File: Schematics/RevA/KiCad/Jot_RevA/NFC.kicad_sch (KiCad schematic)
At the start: 0 parts

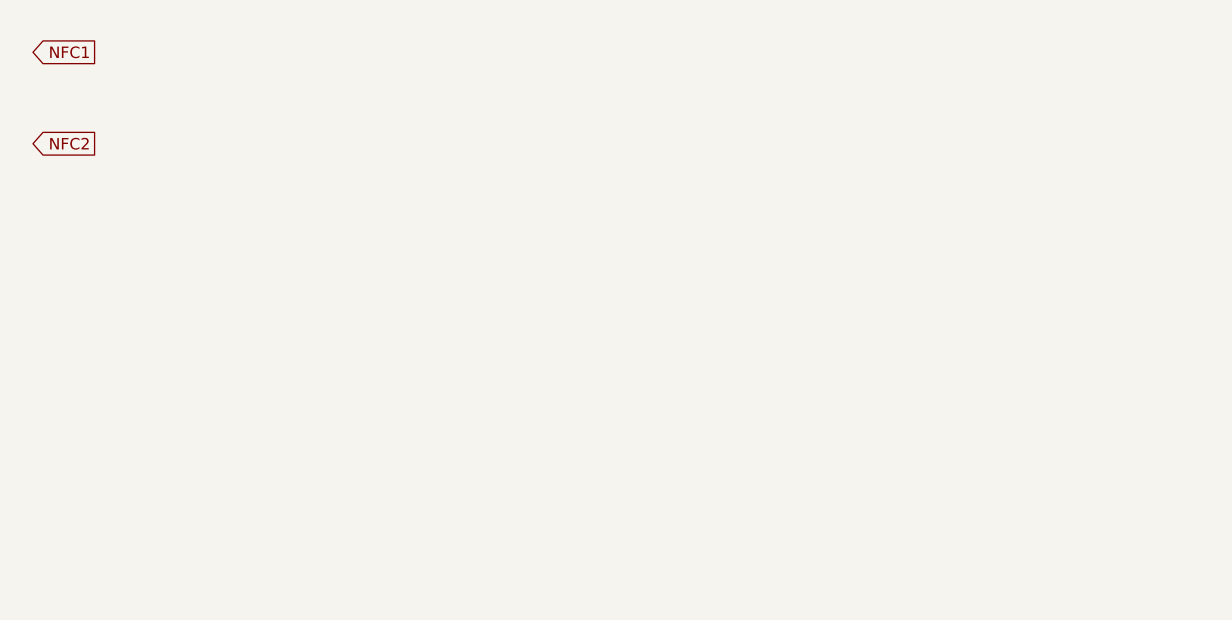
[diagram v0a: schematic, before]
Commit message: NFC sheet: AE1 PCB coil across NFC1/NFC2, C16/C17 180 pF to GND (provisional for ~1.5 uH); title block; BOM row for the NFC caps
Co-Authored-By: Claude Opus 5.5 <noreply@anthropic.com>
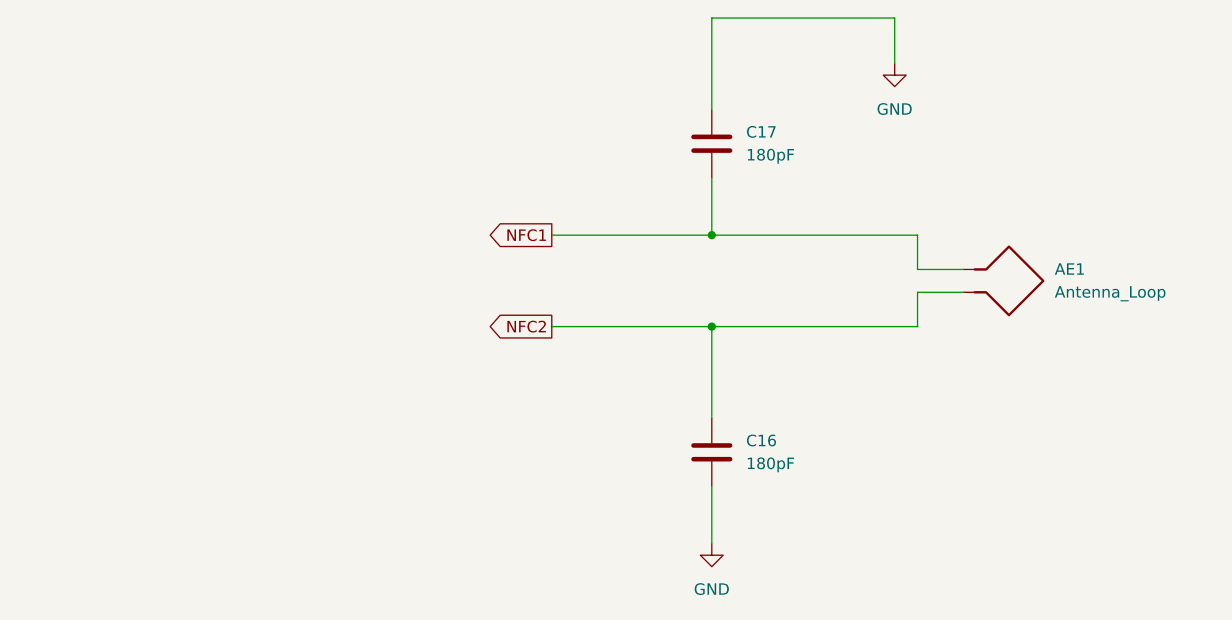
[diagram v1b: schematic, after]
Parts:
- added AE1: Antenna_Loop, symbol Device:Antenna_Loop
- added C16, C17: 180pF, symbol Device:C
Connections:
- net NFC1: now also AE1.1, C17.2
- net NFC2: now also AE1.2, C16.1
- new net GND: C16.2, C17.1

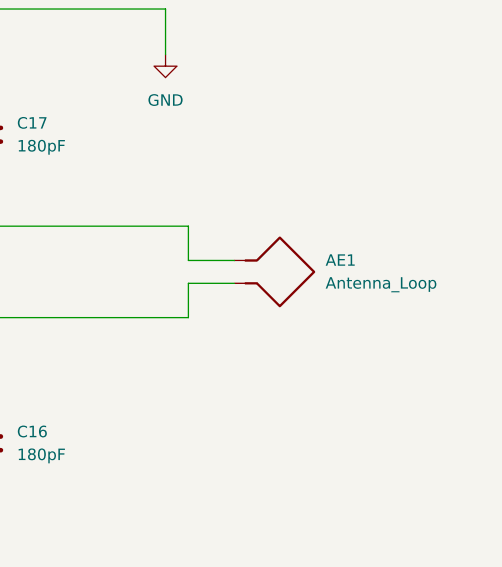
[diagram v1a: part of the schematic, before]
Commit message: NFC sheet: AE1 value 'NFC coil (PCB)'; DRV2605L datasheet with annotations
Co-Authored-By: Claude Opus 5.5 <noreply@anthropic.com>
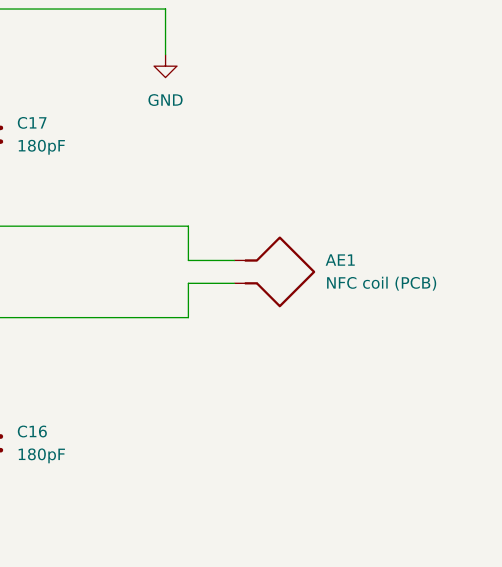
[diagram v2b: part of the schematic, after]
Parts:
- AE1: value Antenna_Loop -> NFC coil (PCB)
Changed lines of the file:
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@@
 			)
 		)
-		(property "Value" "Antenna_Loop"
+		(property "Value" "NFC coil (PCB)"
 			(at 185.42 92.7099 90)
 			(show_name no)

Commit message: Footprints: all resistors (0402, R19 1206) and capacitors (0402, 10 uF 0603) assigned to match the BOM
Co-Authored-By: Claude Opus 5.5 <noreply@anthropic.com>
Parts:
- C16, C17: footprint (none) -> Capacitor_SMD:C_0402_1005Metric
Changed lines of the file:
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@@
 			)
 		)
-		(property "Footprint" ""
+		(property "Footprint" "Capacitor_SMD:C_0402_1005Metric"
 			(at 148.2852 114.3 0)
 			(hide yes)
@@
 			)
 		)
-		(property "Footprint" ""
+		(property "Footprint" "Capacitor_SMD:C_0402_1005Metric"
 			(at 148.2852 80.01 0)
 			(hide yes)
